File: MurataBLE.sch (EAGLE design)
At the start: 43 parts, among them CON1 C-2235, IC1 I-5448, IC3 74LVC1G00DBV, Q1 FC-135 32.7680KA-AG3, Q2 12MHz, SW1 P8073, SW2 P8073, SW3 P8073, U1 IC_BLE_LBCA2HNZYZ-711, X1 TSW-114-02-S-S

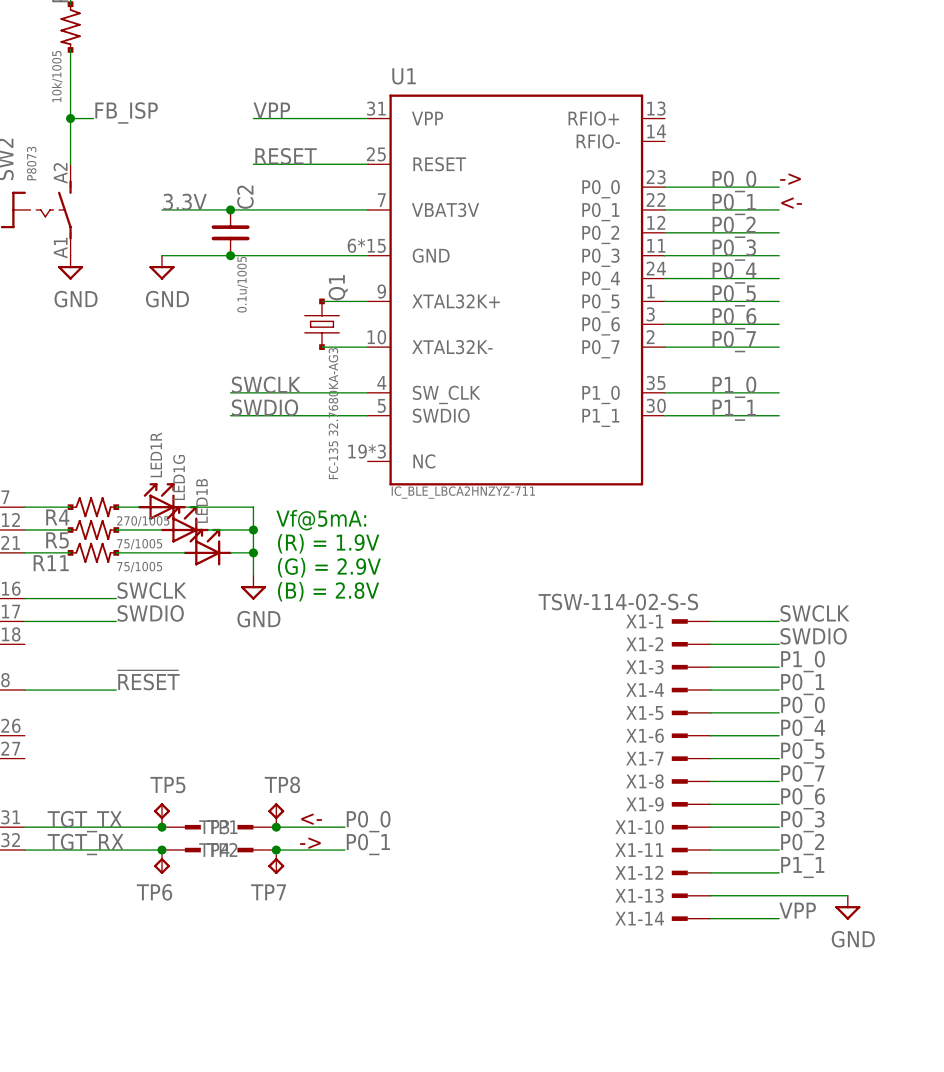
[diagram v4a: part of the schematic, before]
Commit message: [ USB ] UART connection
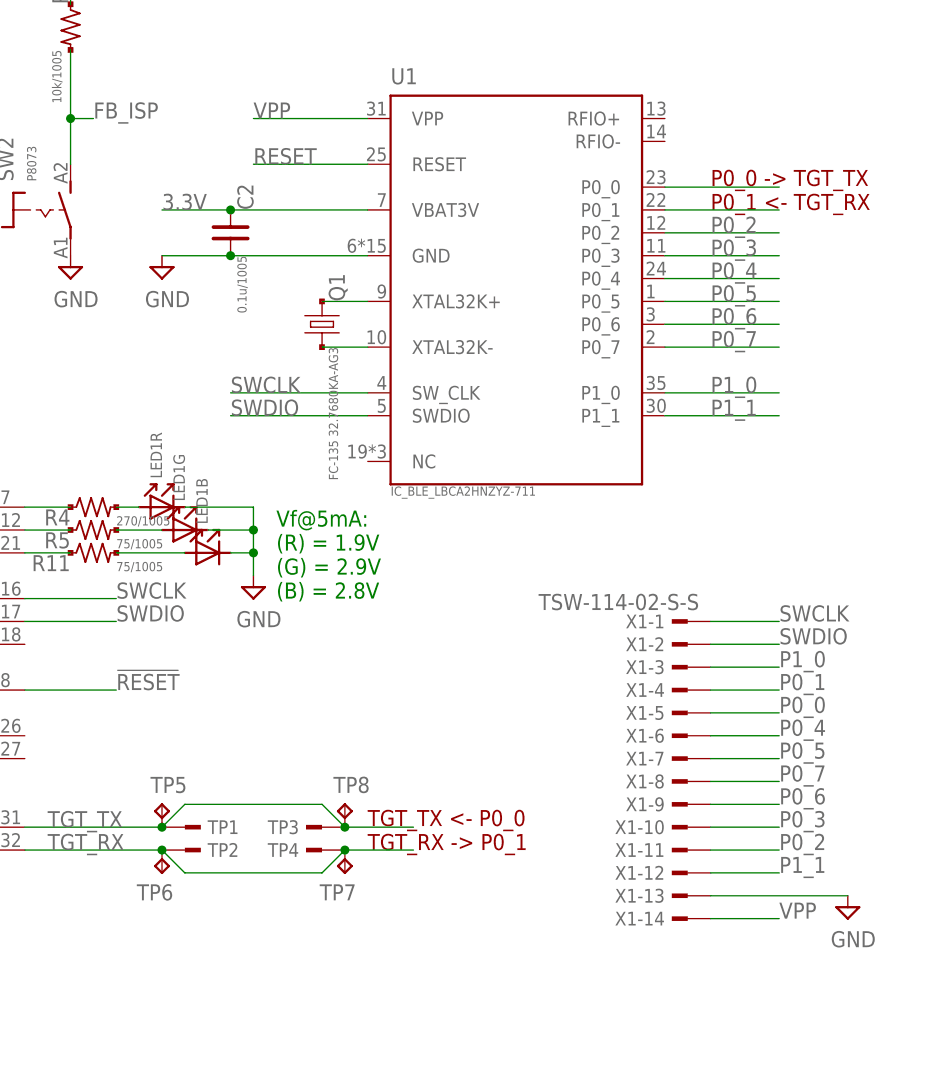
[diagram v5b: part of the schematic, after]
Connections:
- net P0_0: no longer TP3.1, TP8.TP
- net P0_1: no longer TP4.1, TP7.TP
- net TGT_RX: now also TP4.1, TP7.TP
- net TGT_TX: now also TP3.1, TP8.TP
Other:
- note added: "P0_0 -> TGT_TX P0_1 <- TGT_RX"
- note added: "TGT_TX <- P0_0 TGT_RX -> P0_1"
- note removed: "-> <-"
- note removed: "<- ->"
- moved on the sheet: TP3, TP4, TP7, TP8
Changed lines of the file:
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@@
 (G) = 2.9V
 (B) = 2.8V</text>
-<text x="187.96" y="68.58" size="1.778" layer="94">&lt;-
--&gt;</text>
-<text x="241.3" y="139.7" size="1.778" layer="94">-&gt;
-&lt;-</text>
+<text x="195.58" y="68.58" size="1.778" layer="94">TGT_TX &lt;- P0_0
+TGT_RX -&gt; P0_1</text>
+<text x="233.68" y="139.7" size="1.778" layer="94">P0_0 -&gt; TGT_TX
+P0_1 &lt;- TGT_RX</text>
 <text x="226.06" y="20.32" size="2.54" layer="94">CC-BY-SA</text>
 </plain>
@@
 <instance part="TP5" gate="G$1" x="172.72" y="73.66"/>
 <instance part="TP6" gate="G$1" x="172.72" y="66.04" rot="R180"/>
-<instance part="TP7" gate="G$1" x="185.42" y="66.04" rot="R180"/>
-<instance part="TP8" gate="G$1" x="185.42" y="73.66"/>
+<instance part="TP7" gate="G$1" x="193.04" y="66.04" rot="R180"/>
+<instance part="TP8" gate="G$1" x="193.04" y="73.66"/>
 <instance part="X1" gate="-1" x="231.14" y="93.98" rot="MR0"/>
 <instance part="X1" gate="-2" x="231.14" y="91.44" rot="MR0"/>
@@
 <instance part="TP1" gate="1" x="175.26" y="71.12"/>
 <instance part="TP2" gate="1" x="175.26" y="68.58"/>
-<instance part="TP3" gate="1" x="182.88" y="71.12" rot="R180"/>
-<instance part="TP4" gate="1" x="182.88" y="68.58" rot="R180"/>
+<instance part="TP3" gate="1" x="190.5" y="71.12" rot="R180"/>
+<instance part="TP4" gate="1" x="190.5" y="68.58" rot="R180"/>
 </instances>
 <busses>
@@
 <pinref part="U1" gate="G$1" pin="P0_0"/>
 <wire x1="241.3" y1="142.24" x2="228.6" y2="142.24" width="0.1524" layer="91"/>
-<label x="233.68" y="142.24" size="1.778" layer="95"/>
 </segment>
 <segment>
@@
 <pinref part="X1" gate="-5" pin="1"/>
 </segment>
-<segment>
-<wire x1="193.04" y1="71.12" x2="185.42" y2="71.12" width="0.1524" layer="91"/>
-<label x="193.04" y="71.12" size="1.778" layer="95"/>
-<pinref part="TP8" gate="G$1" pin="TP"/>
-<junction x="185.42" y="71.12"/>
-<pinref part="TP3" gate="1" pin="1"/>
-</segment>
 </net>
 <net name="P0_1" class="0">
@@
 <pinref part="U1" gate="G$1" pin="P0_1"/>
 <wire x1="241.3" y1="139.7" x2="228.6" y2="139.7" width="0.1524" layer="91"/>
-<label x="233.68" y="139.7" size="1.778" layer="95"/>
 </segment>
 <segment>
@@
 <label x="241.3" y="86.36" size="1.778" layer="95"/>
 <pinref part="X1" gate="-4" pin="1"/>
-</segment>
-<segment>
-<wire x1="193.04" y1="68.58" x2="185.42" y2="68.58" width="0.1524" layer="91"/>
-<label x="193.04" y="68.58" size="1.778" layer="95"/>
-<pinref part="TP7" gate="G$1" pin="TP"/>
-<junction x="185.42" y="68.58"/>
-<pinref part="TP4" gate="1" pin="1"/>
 </segment>
 </net>
@@
 <junction x="172.72" y="71.12"/>
 <pinref part="TP1" gate="1" pin="1"/>
+<wire x1="200.66" y1="71.12" x2="193.04" y2="71.12" width="0.1524" layer="91"/>
+<pinref part="TP8" gate="G$1" pin="TP"/>
+<junction x="193.04" y="71.12"/>
+<pinref part="TP3" gate="1" pin="1"/>
+<wire x1="172.72" y1="71.12" x2="175.26" y2="73.66" width="0.1524" layer="91"/>
+<wire x1="175.26" y1="73.66" x2="190.5" y2="73.66" width="0.1524" layer="91"/>
+<wire x1="190.5" y1="73.66" x2="193.04" y2="71.12" width="0.1524" layer="91"/>
+</segment>
+</net>
+<net name="N$4" class="0">
+<segment>
+<pinref part="R6" gate="G$1" pin="2"/>
+<pinref part="IC2" gate="G$1" pin="USB_VBUS"/>
+<wire x1="101.6" y1="88.9" x2="111.76" y2="88.9" width="0.1524" layer="91"/>
+</segment>
+</net>
+<net name="N$5" class="0">
+<segment>
+<pinref part="R9" gate="G$1" pin="2"/>
+<pinref part="IC2" gate="G$1" pin="IF_NRESET"/>
+<wire x1="101.6" y1="106.68" x2="111.76" y2="106.68" width="0.1524" layer="91"/>
+</segment>
+</net>
+<net name="VPP" class="0">
+<segment>
+<pinref part="U1" gate="G$1" pin="VPP"/>
+<wire x1="182.88" y1="149.86" x2="195.58" y2="149.86" width="0.1524" layer="91"/>
+<label x="182.88" y="149.86" size="1.778" layer="95"/>
+</segment>
+<segment>
+<label x="241.3" y="60.96" size="1.778" layer="95"/>
+<wire x1="233.68" y1="60.96" x2="241.3" y2="60.96" width="0.1524" layer="91"/>
+<pinref part="X1" gate="-14" pin="1"/>
+</segment>
+</net>
+<net name="N$6" class="0">
+<segment>
+<pinref part="TR1" gate="G$1" pin="D"/>
+<pinref part="R10" gate="G$1" pin="1"/>
+<wire x1="48.26" y1="114.3" x2="48.26" y2="109.22" width="0.1524" layer="91"/>
+</segment>
+</net>
+<net name="N$7" class="0">
+<segment>
+<pinref part="IC2" gate="G$1" pin="USB_SCON"/>
+<wire x1="111.76" y1="86.36" x2="81.28" y2="86.36" width="0.1524" layer="91"/>
+<wire x1="81.28" y1="86.36" x2="81.28" y2="121.92" width="0.1524" layer="91"/>
+<pinref part="TR1" gate="G$1" pin="G"/>
+<wire x1="81.28" y1="121.92" x2="53.34" y2="121.92" width="0.1524" layer="91"/>
+</segment>
+</net>
+<net name="N$8" class="0">
+<segment>
+<pinref part="IC2" gate="G$1" pin="LED_MSD"/>
+<pinref part="R4" gate="G$1" pin="1"/>
+<wire x1="157.48" y1="106.68" x2="162.56" y2="106.68" width="0.1524" layer="91"/>
+</segment>
+</net>
+<net name="N$9" class="0">
+<segment>
+<pinref part="IC2" gate="G$1" pin="LED_HID"/>
+<pinref part="R5" gate="G$1" pin="1"/>
+<wire x1="157.48" y1="104.14" x2="162.56" y2="104.14" width="0.1524" layer="91"/>
+</segment>
+</net>
+<net name="N$10" class="0">
+<segment>
+<pinref part="IC2" gate="G$1" pin="LED_UART"/>
+<pinref part="R11" gate="G$1" pin="1"/>
+<wire x1="157.48" y1="101.6" x2="162.56" y2="101.6" width="0.1524" layer="91"/>
+</segment>
+</net>
+<net name="N$11" class="0">
+<segment>
+<pinref part="R4" gate="G$1" pin="2"/>
+<wire x1="167.64" y1="106.68" x2="170.18" y2="106.68" width="0.1524" layer="91"/>
+<pinref part="LED1" gate="R" pin="A"/>
+</segment>
+</net>
+<net name="N$12" class="0">
+<segment>
+<pinref part="R5" gate="G$1" pin="2"/>
+<wire x1="172.72" y1="104.14" x2="167.64" y2="104.14" width="0.1524" layer="91"/>
+<pinref part="LED1" gate="G" pin="A"/>
+</segment>
+</net>
+<net name="N$13" class="0">
+<segment>
+<pinref part="R11" gate="G$1" pin="2"/>
+<wire x1="167.64" y1="101.6" x2="175.26" y2="101.6" width="0.1524" layer="91"/>
+<pinref part="LED1" gate="B" pin="A"/>
 </segment>
 </net>
 <net name="TGT_RX" class="0">
 <segment>
+<wire x1="200.66" y1="68.58" x2="193.04" y2="68.58" width="0.1524" layer="91"/>
+<pinref part="TP7" gate="G$1" pin="TP"/>
+<junction x="193.04" y="68.58"/>
+<pinref part="TP4" gate="1" pin="1"/>
 <pinref part="IC2" gate="G$1" pin="TGT_RX"/>
 <label x="160.02" y="68.58" size="1.778" layer="95"/>
@@
 <junction x="172.72" y="68.58"/>
 <pinref part="TP2" gate="1" pin="1"/>
-</segment>
-</net>
-<net name="N$4" class="0">
-<segment>
-<pinref part="R6" gate="G$1" pin="2"/>
-<pinref part="IC2" gate="G$1" pin="USB_VBUS"/>
-<wire x1="101.6" y1="88.9" x2="111.76" y2="88.9" width="0.1524" layer="91"/>
-</segment>
-</net>
-<net name="N$5" class="0">
-<segment>
-<pinref part="R9" gate="G$1" pin="2"/>
-<pinref part="IC2" gate="G$1" pin="IF_NRESET"/>
-<wire x1="101.6" y1="106.68" x2="111.76" y2="106.68" width="0.1524" layer="91"/>
-</segment>
-</net>
-<net name="VPP" class="0">
-<segment>
-<pinref part="U1" gate="G$1" pin="VPP"/>
-<wire x1="182.88" y1="149.86" x2="195.58" y2="149.86" width="0.1524" layer="91"/>
-<label x="182.88" y="149.86" size="1.778" layer="95"/>
-</segment>
-<segment>
-<label x="241.3" y="60.96" size="1.778" layer="95"/>
-<wire x1="233.68" y1="60.96" x2="241.3" y2="60.96" width="0.1524" layer="91"/>
-<pinref part="X1" gate="-14" pin="1"/>
-</segment>
-</net>
-<net name="N$6" class="0">
-<segment>
-<pinref part="TR1" gate="G$1" pin="D"/>
-<pinref part="R10" gate="G$1" pin="1"/>
-<wire x1="48.26" y1="114.3" x2="48.26" y2="109.22" width="0.1524" layer="91"/>
-</segment>
-</net>
-<net name="N$7" class="0">
-<segment>
-<pinref part="IC2" gate="G$1" pin="USB_SCON"/>
-<wire x1="111.76" y1="86.36" x2="81.28" y2="86.36" width="0.1524" layer="91"/>
-<wire x1="81.28" y1="86.36" x2="81.28" y2="121.92" width="0.1524" layer="91"/>
-<pinref part="TR1" gate="G$1" pin="G"/>
-<wire x1="81.28" y1="121.92" x2="53.34" y2="121.92" width="0.1524" layer="91"/>
-</segment>
-</net>
-<net name="N$8" class="0">
-<segment>
-<pinref part="IC2" gate="G$1" pin="LED_MSD"/>
-<pinref part="R4" gate="G$1" pin="1"/>
-<wire x1="157.48" y1="106.68" x2="162.56" y2="106.68" width="0.1524" layer="91"/>
-</segment>
-</net>
-<net name="N$9" class="0">
-<segment>
-<pinref part="IC2" gate="G$1" pin="LED_HID"/>
-<pinref part="R5" gate="G$1" pin="1"/>
-<wire x1="157.48" y1="104.14" x2="162.56" y2="104.14" width="0.1524" layer="91"/>
-</segment>
-</net>
-<net name="N$10" class="0">
-<segment>
-<pinref part="IC2" gate="G$1" pin="LED_UART"/>
-<pinref part="R11" gate="G$1" pin="1"/>
-<wire x1="157.48" y1="101.6" x2="162.56" y2="101.6" width="0.1524" layer="91"/>
-</segment>
-</net>
-<net name="N$11" class="0">
-<segment>
-<pinref part="R4" gate="G$1" pin="2"/>
-<wire x1="167.64" y1="106.68" x2="170.18" y2="106.68" width="0.1524" layer="91"/>
-<pinref part="LED1" gate="R" pin="A"/>
-</segment>
-</net>
-<net name="N$12" class="0">
-<segment>
-<pinref part="R5" gate="G$1" pin="2"/>
-<wire x1="172.72" y1="104.14" x2="167.64" y2="104.14" width="0.1524" layer="91"/>
-<pinref part="LED1" gate="G" pin="A"/>
-</segment>
-</net>
-<net name="N$13" class="0">
-<segment>
-<pinref part="R11" gate="G$1" pin="2"/>
-<wire x1="167.64" y1="101.6" x2="175.26" y2="101.6" width="0.1524" layer="91"/>
-<pinref part="LED1" gate="B" pin="A"/>
-</segment>
-</net>
+<wire x1="193.04" y1="68.58" x2="190.5" y2="66.04" width="0.1524" layer="91"/>
+<wire x1="190.5" y1="66.04" x2="175.26" y2="66.04" width="0.1524" layer="91"/>
+<wire x1="175.26" y1="66.04" x2="172.72" y2="68.58" width="0.1524" layer="91"/>
+</segment>
+</net>

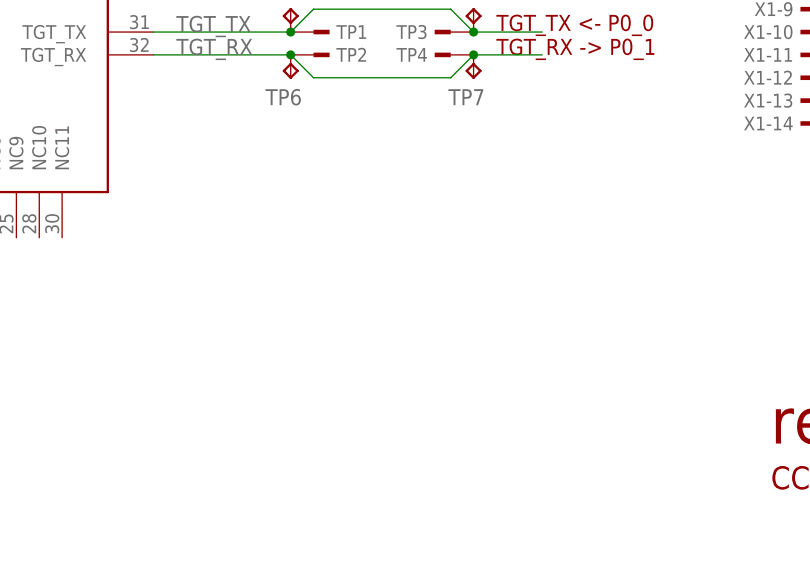
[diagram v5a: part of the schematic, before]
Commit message: [ USB ] Fiducials; panel direction
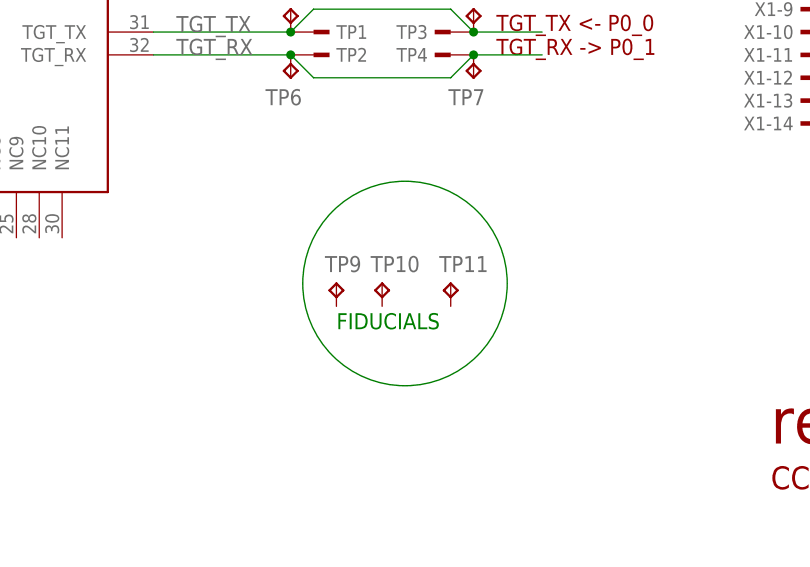
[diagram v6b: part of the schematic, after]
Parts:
- added TP10, TP11, TP9: TPTP08R, testpad_local:TPTP08R
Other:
- note added: "FIDUCIALS"
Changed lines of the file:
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@@
 <part name="TP3" library="mylib" deviceset="TESTPAD" device=""/>
 <part name="TP4" library="mylib" deviceset="TESTPAD" device=""/>
+<part name="TP9" library="testpad_local" deviceset="TP" device="TP08R" value="TPTP08R"/>
+<part name="TP10" library="testpad_local" deviceset="TP" device="TP08R" value="TPTP08R"/>
+<part name="TP11" library="testpad_local" deviceset="TP" device="TP08R" value="TPTP08R"/>
 </parts>
 <sheets>
@@
 P0_1 &lt;- TGT_RX</text>
 <text x="226.06" y="20.32" size="2.54" layer="94">CC-BY-SA</text>
+<text x="177.8" y="38.1" size="1.778" layer="91">FIDUCIALS</text>
+<circle x="185.42" y="43.18" radius="11.359225" width="0.1524" layer="91"/>
 </plain>
 <instances>
@@
 <instance part="TP3" gate="1" x="190.5" y="71.12" rot="R180"/>
 <instance part="TP4" gate="1" x="190.5" y="68.58" rot="R180"/>
+<instance part="TP9" gate="G$1" x="177.8" y="43.18"/>
+<instance part="TP10" gate="G$1" x="182.88" y="43.18"/>
+<instance part="TP11" gate="G$1" x="190.5" y="43.18"/>
 </instances>
 <busses>
